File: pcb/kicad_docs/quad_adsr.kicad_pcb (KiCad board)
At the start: 4 copper layers, 71.1 x 99.1 mm, 197 parts, among them J1 PJ301M-12, J10 gate_3_in, J11 trigger_3_in, J12 gate_4_in, J13 trigger_4_in, J14 SWD_header, J2 PJ301M-12, J3 PJ301M-12, J4 PJ301M-12, J5 power_in, J6 gate_1_i n, J7 trigger_1_in, J8 gate_2_in, J9 trigger_2_in, Q1 MMBT3904, Q10 MMBT3904, Q11 MMBT3904, Q12 MMBT3904, Q2 MMBT3904, Q3 MMBT3904, Q4 MMBT3904, Q5 MMBT3904, Q6 MMBT3904, Q7 MMBT3904, Q8 MMBT3904, Q9 MMBT3904, U1 HDSP-7503, U10 MCP4822, U11 TL072, U12 STM32F405RGTx, U13 24LC32, U2 74HC595, U3 HDSP-7503, U4 HDSP-7503, U5 HDSP-7503, U6 74HC595, U7 AMS1117-3.3, U8 TL072, U9 MCP4822

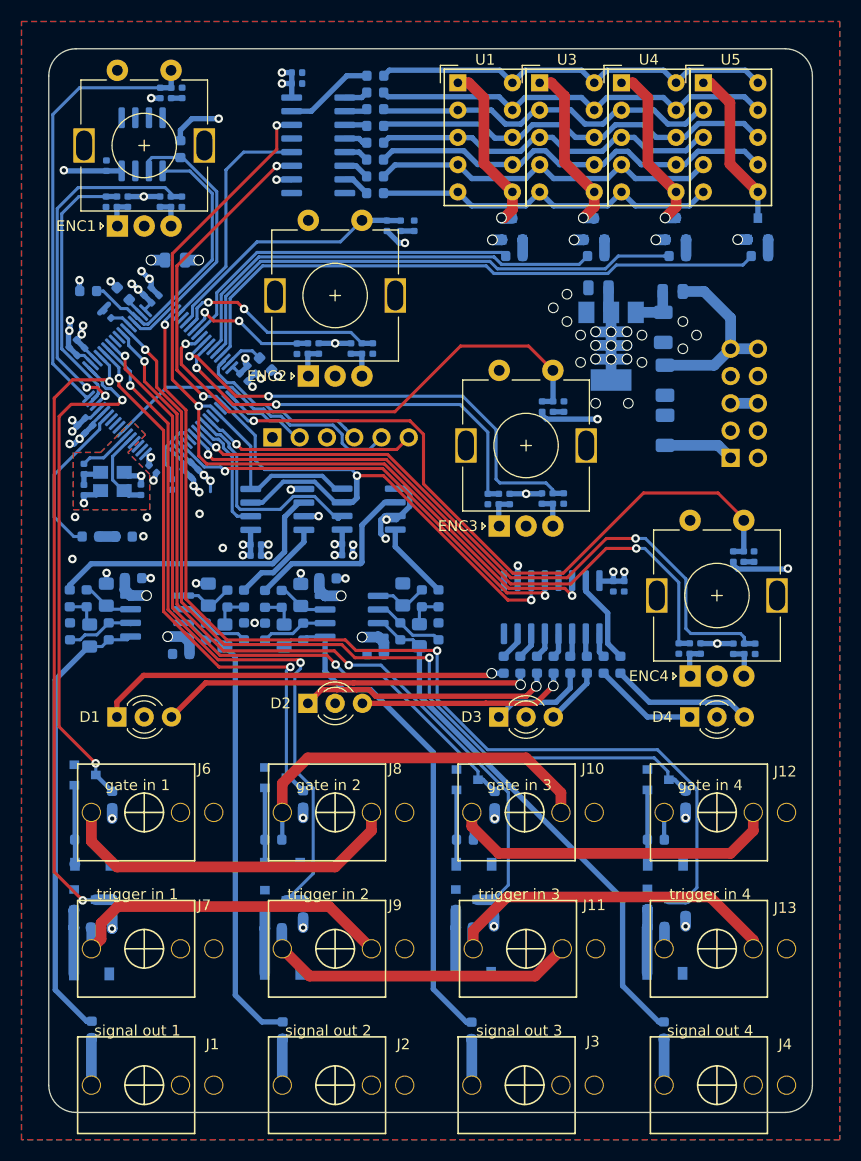
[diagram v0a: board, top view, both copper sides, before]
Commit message: add front panel, rearrange directories
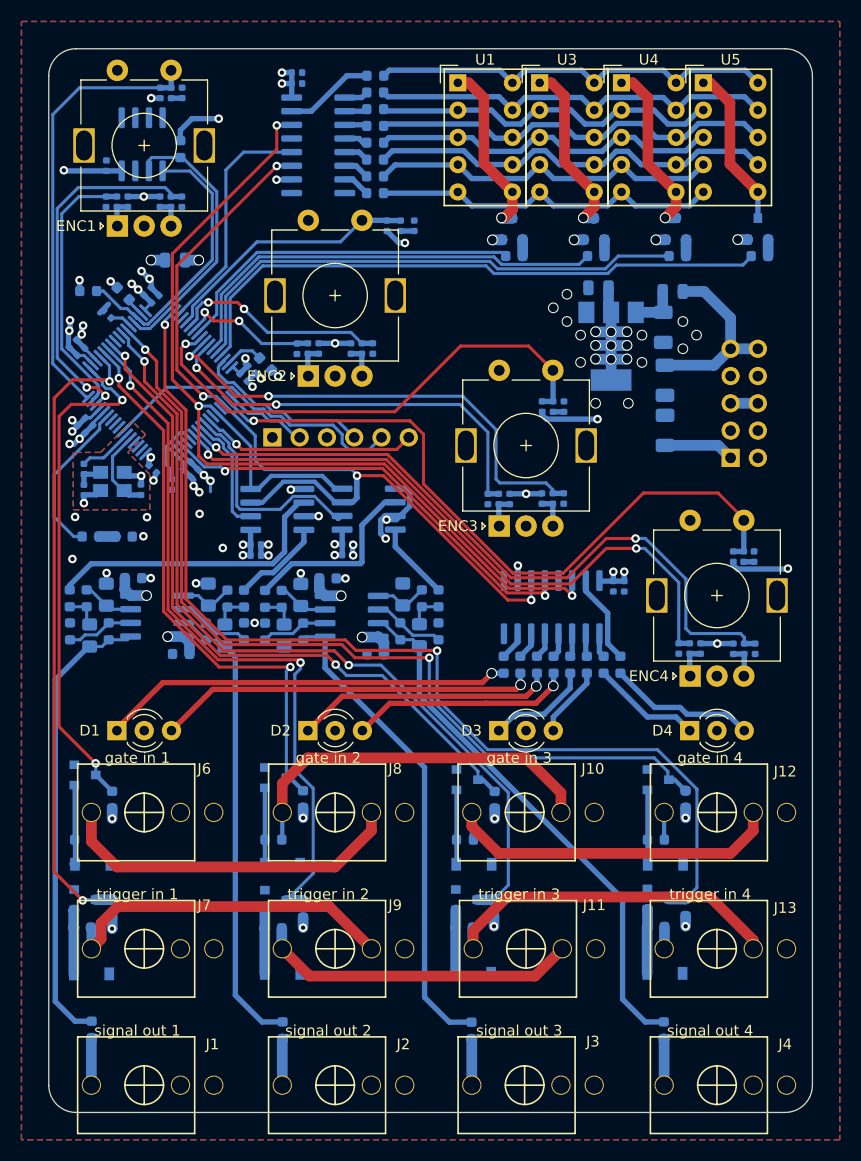
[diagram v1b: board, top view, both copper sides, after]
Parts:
- moved D2 2.54 mm to (100.3, 114.3)
- moved D1 1.27 mm to (82.5, 114.3)
- moved D3 1.27 mm to (118.1, 114.3)
- moved D4 1.27 mm to (135.9, 114.3)
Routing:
- net Net-(D3-Pad3): track 5.37 -> 6.64 mm
- net Net-(D2-Pad3): track 19.6 -> 20.7 mm
- net /spi_dacs_and_level_shifters/10vp_adsr_4_out: track 49.4 -> 50.1 mm
- net /spi_dacs_and_level_shifters/10vp_adsr_1_out: track 42.2 -> 42.8 mm
- net /spi_dacs_and_level_shifters/10vp_adsr_3_out: track 47.5 -> 46.9 mm
- net Net-(D2-Pad1): track 23.7 -> 24.2 mm
- net Net-(D4-Pad1): track 9.70 -> 10.2 mm
- net Net-(D3-Pad1): track 9.15 -> 9.68 mm
- net Net-(D4-Pad3): track 13.2 -> 13.8 mm

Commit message: add github url and rev info to silk
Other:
- board text added: "github.com/JordanAceto/quad_ADSR_board rev 0 2020-08-05"

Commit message: small pcb treaks
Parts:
- R25, R34, R35, R36: value 3k3 -> 10k
- R26, R27, R28, R29, R30, R31, R32, R33, R37, R38, R39, R40, R41, R42, R43, R44: value 330 -> 390
- moved C51 9.78 mm to (138.8, 73.4), turned to 0 degrees
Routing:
- net +12V: track 104.9 -> 98.2 mm
- net /stmf32/gate_1_in: track 49.0 -> 48.1 mm
- net /encoders/enc_3_sw_out: track 47.6 -> 46.9 mm
- net GND: vias 52 -> 62
